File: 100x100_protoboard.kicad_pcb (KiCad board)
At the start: 2 copper layers, 97.8 x 96.5 mm, 418 parts, among them CON1 BARREL_JACK, CON2 USB_FEMALE_WITH_ID, CON3 USB_FEMALE_WITH_ID, J1 INTERCONNECT_1X03, J10 INTERCONNECT_1X03, J11 INTERCONNECT_1X03, J12 INTERCONNECT_1X03, J13 INTERCONNECT_1X03, J14 INTERCONNECT_1X03, J15 INTERCONNECT_1X03, J16 INTERCONNECT_1X03, J17 INTERCONNECT_1X03, J18 INTERCONNECT_1X03, J19 INTERCONNECT_1X03, J2 INTERCONNECT_1X03, J20 INTERCONNECT_1X03, J21 INTERCONNECT_1X03, J22 INTERCONNECT_1X03, J23 INTERCONNECT_1X03, J24 INTERCONNECT_1X03, J25 INTERCONNECT_1X03, J26 INTERCONNECT_1X03, J27 INTERCONNECT_1X03, J28 INTERCONNECT_1X03, J29 INTERCONNECT_1X03, J3 INTERCONNECT_1X03, J30 INTERCONNECT_1X03, J31 INTERCONNECT_1X03, J32 INTERCONNECT_1X03, J33 INTERCONNECT_1X03, J34 INTERCONNECT_1X03, J35 INTERCONNECT_1X03, J36 INTERCONNECT_1X03, J37 INTERCONNECT_1X03, J38 INTERCONNECT_1X03, J39 INTERCONNECT_1X03, J4 INTERCONNECT_1X03, J40 INTERCONNECT_1X03, J41 INTERCONNECT_1X03, J42 INTERCONNECT_1X03, J43 INTERCONNECT_1X03, J44 INTERCONNECT_1X03, J45 INTERCONNECT_1X03, J46 INTERCONNECT_1X03, J47 INTERCONNECT_1X03, J48 INTERCONNECT_1X03, J49 INTERCONNECT_1X03, J5 INTERCONNECT_1X03, J50 INTERCONNECT_1X03, J51 INTERCONNECT_1X03, J52 INTERCONNECT_1X03, J53 INTERCONNECT_1X03, J54 INTERCONNECT_1X03, J55 INTERCONNECT_1X03, J56 INTERCONNECT_1X03, J57 INTERCONNECT_1X03, J58 INTERCONNECT_1X03, J59 INTERCONNECT_1X03, J6 INTERCONNECT_1X03, J60 INTERCONNECT_1X03, J61 INTERCONNECT_1X03, J62 INTERCONNECT_1X03, J63 INTERCONNECT_1X03, J64 INTERCONNECT_1X03, J65 INTERCONNECT_1X02, J7 INTERCONNECT_1X03, J8 INTERCONNECT_1X03, J9 INTERCONNECT_1X03, P1 CONN_5, P1 CONN_8X2, P2 CONN_8X2, U1 LM7805CT

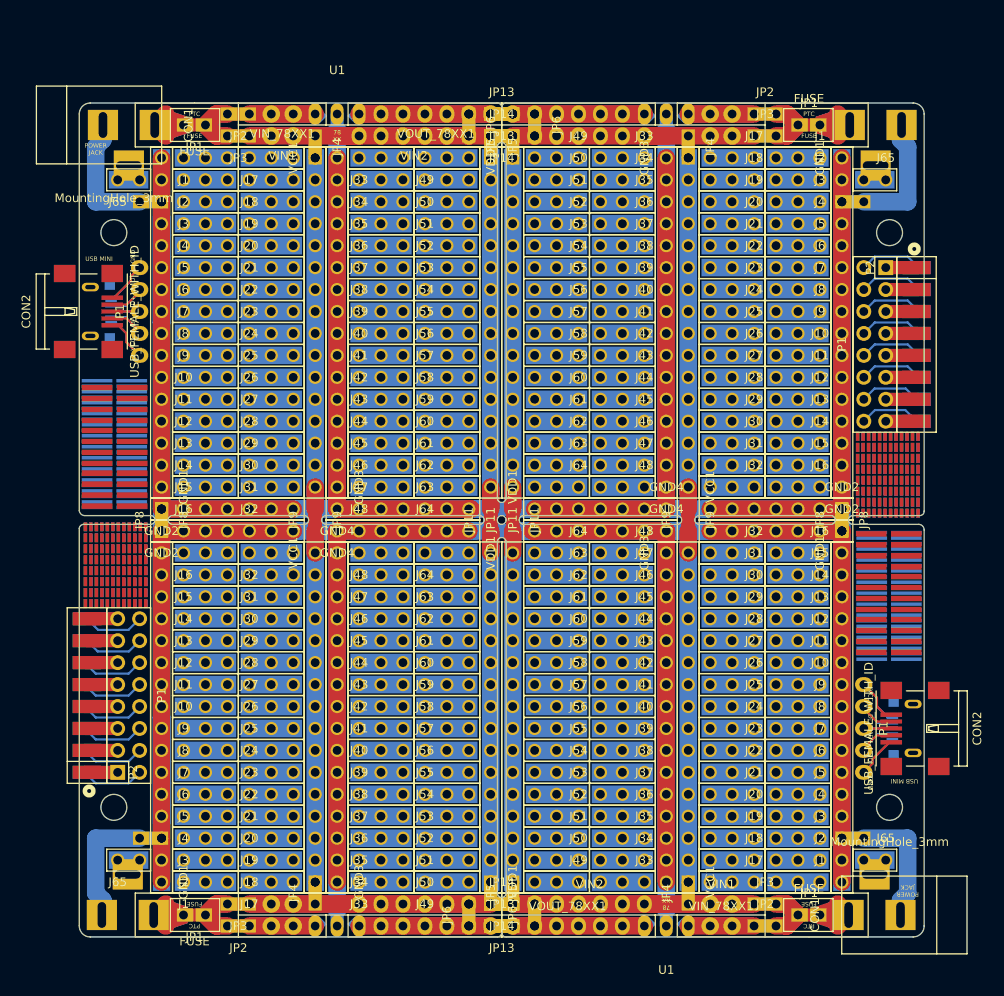
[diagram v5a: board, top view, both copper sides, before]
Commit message: rounded some corners
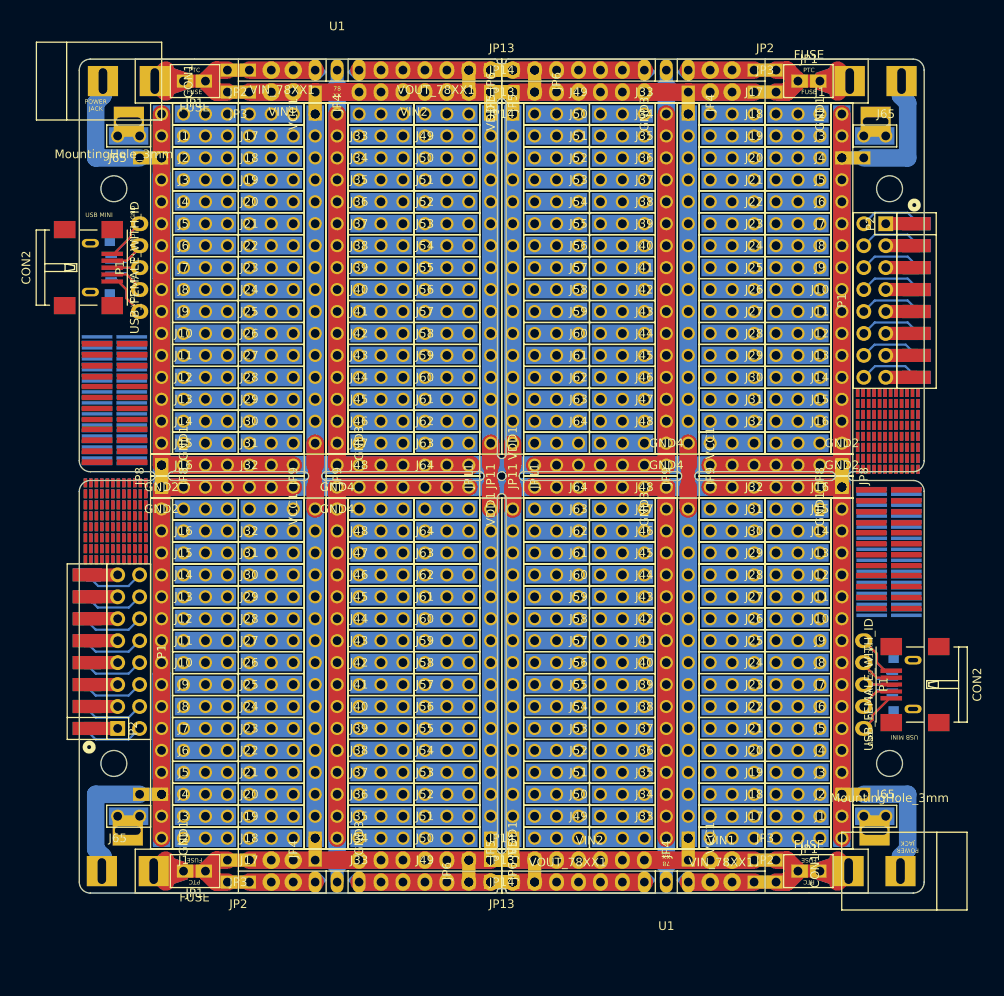
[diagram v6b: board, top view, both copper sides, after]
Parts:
- removed the C1 at (101.6, 32.8)
- removed the C1 at (101.6, 124.7)
- removed the C2 at (99.1, 32.8)
- removed the C2 at (99.1, 124.7)
- removed the CON1 at (127.8, 33.0)
- removed the CON1 at (127.6, 124.5)
- removed the CON1 at (34.8, 124.5)
- removed the F1 at (116.8, 33.0)
- removed the F1 at (116.8, 124.5)
- removed the F2 at (116.8, 33.0)
- removed the F2 at (116.8, 124.5)
- removed the GND1 at (120.7, 36.8)
- removed the GND1 at (120.7, 82.5)
- removed the GND2 at (120.7, 77.5)
- removed the GND2 at (120.7, 80.0)
- removed the GND3 at (100.3, 36.8)
- removed the GND3 at (100.3, 82.5)
- removed the GND4 at (100.3, 77.5)
- removed the GND4 at (100.3, 80.0)
- removed the J1 at (118.1, 36.8)
- removed the J1 at (118.1, 120.7)
- removed the J10 at (118.1, 59.7)
- removed the J10 at (118.1, 97.8)
- removed the J11 at (118.1, 62.2)
- removed the J11 at (118.1, 95.2)
- removed the J12 at (118.1, 64.8)
- removed the J12 at (118.1, 92.7)
- removed the J13 at (118.1, 67.3)
- removed the J13 at (118.1, 90.2)
- removed the J14 at (118.1, 69.8)
- removed the J14 at (118.1, 87.6)
- removed the J15 at (118.1, 72.4)
- removed the J15 at (118.1, 85.1)
- removed the J16 at (118.1, 74.9)
- removed the J16 at (118.1, 82.5)
- removed the J17 at (110.5, 36.8)
- removed the J17 at (110.5, 120.7)
- removed the J18 at (110.5, 39.4)
- removed the J18 at (110.5, 118.1)
- removed the J19 at (110.5, 41.9)
- removed the J19 at (110.5, 115.6)
- removed the J2 at (118.1, 39.4)
- removed the J2 at (118.1, 118.1)
- removed the J20 at (110.5, 44.5)
- removed the J20 at (110.5, 113.0)
- removed the J21 at (110.5, 47.0)
- removed the J21 at (110.5, 110.5)
- removed the J22 at (110.5, 49.5)
- removed the J22 at (110.5, 108.0)
- removed the J23 at (110.5, 52.1)
- removed the J23 at (110.5, 105.4)
- removed the J24 at (110.5, 54.6)
- removed the J24 at (110.5, 102.9)
- removed the J25 at (110.5, 57.1)
- removed the J25 at (110.5, 100.3)
- removed the J26 at (110.5, 59.7)
- removed the J26 at (110.5, 97.8)
- removed the J27 at (110.5, 62.2)
- removed the J27 at (110.5, 95.2)
- removed the J28 at (110.5, 64.8)
- removed the J28 at (110.5, 92.7)
- removed the J29 at (110.5, 67.3)
- removed the J29 at (110.5, 90.2)
- removed the J3 at (118.1, 41.9)
- removed the J3 at (118.1, 115.6)
- removed the J30 at (110.5, 69.8)
- removed the J30 at (110.5, 87.6)
- removed the J31 at (110.5, 72.4)
- removed the J31 at (110.5, 85.1)
- removed the J32 at (110.5, 74.9)
- removed the J32 at (110.5, 82.5)
- removed the J33 at (97.8, 36.8)
- removed the J33 at (97.8, 120.7)
- removed the J34 at (97.8, 39.4)
- removed the J34 at (97.8, 118.1)
- removed the J35 at (97.8, 41.9)
- removed the J35 at (97.8, 115.6)
- removed the J36 at (97.8, 44.5)
- removed the J36 at (97.8, 113.0)
- removed the J37 at (97.8, 47.0)
- removed the J37 at (97.8, 110.5)
- removed the J38 at (97.8, 49.5)
- removed the J38 at (97.8, 108.0)
- removed the J39 at (97.8, 52.1)
- removed the J39 at (97.8, 105.4)
- removed the J4 at (118.1, 44.5)
- removed the J4 at (118.1, 113.0)
- removed the J40 at (97.8, 54.6)
- removed the J40 at (97.8, 102.9)
- removed the J41 at (97.8, 57.1)
- removed the J41 at (97.8, 100.3)
- removed the J42 at (97.8, 59.7)
- removed the J42 at (97.8, 97.8)
- removed the J43 at (97.8, 62.2)
- removed the J43 at (97.8, 95.2)
- removed the J44 at (97.8, 64.8)
- removed the J44 at (97.8, 92.7)
- removed the J45 at (97.8, 67.3)
- removed the J45 at (97.8, 90.2)
- removed the J46 at (97.8, 69.8)
- removed the J46 at (97.8, 87.6)
- removed the J47 at (97.8, 72.4)
- removed the J47 at (97.8, 85.1)
- removed the J48 at (97.8, 74.9)
- removed the J48 at (97.8, 82.5)
- removed the J49 at (90.2, 36.8)
- removed the J49 at (90.2, 120.7)
- removed the J5 at (118.1, 47.0)
- removed the J5 at (118.1, 110.5)
- removed the J50 at (90.2, 39.4)
- removed the J50 at (90.2, 118.1)
- removed the J51 at (90.2, 41.9)
- removed the J51 at (90.2, 115.6)
- removed the J52 at (90.2, 44.5)
- removed the J52 at (90.2, 113.0)
- removed the J53 at (90.2, 47.0)
- removed the J53 at (90.2, 110.5)
- removed the J54 at (90.2, 49.5)
- removed the J54 at (90.2, 108.0)
- removed the J55 at (90.2, 52.1)
- removed the J55 at (90.2, 105.4)
- removed the J56 at (90.2, 54.6)
- removed the J56 at (90.2, 102.9)
- removed the J57 at (90.2, 57.1)
- removed the J57 at (90.2, 100.3)
- removed the J58 at (90.2, 59.7)
- removed the J58 at (90.2, 97.8)
- removed the J59 at (90.2, 62.2)
- removed the J59 at (90.2, 95.2)
- removed the J6 at (118.1, 49.5)
- removed the J6 at (118.1, 108.0)
- removed the J60 at (90.2, 64.8)
- removed the J60 at (90.2, 92.7)
- removed the J61 at (90.2, 67.3)
- removed the J61 at (90.2, 90.2)
- removed the J62 at (90.2, 69.8)
- removed the J62 at (90.2, 87.6)
- removed the J63 at (90.2, 72.4)
- removed the J63 at (90.2, 85.1)
- removed the J64 at (90.2, 74.9)
- removed the J64 at (90.2, 82.5)
- removed the J65 at (125.7, 39.4)
- removed the J65 at (125.7, 118.1)
- removed the J7 at (118.1, 52.1)
- removed the J7 at (118.1, 105.4)
- removed the J8 at (118.1, 54.6)
- removed the J8 at (118.1, 102.9)
- removed the J9 at (118.1, 57.1)
- removed the J9 at (118.1, 100.3)
- removed the JP1 at (116.8, 33.0)
- removed the JP1 at (116.8, 124.5)
- removed the JP10 at (82.5, 78.7) (x2)
- removed the JP11 at (82.5, 78.7) (x2)
- removed the JP12 at (81.3, 77.5)
- removed the JP12 at (81.3, 80.0)
- removed the JP13 at (81.3, 31.8)
- removed the JP13 at (81.3, 125.7)
- removed the JP14 at (81.3, 34.3)
- removed the JP14 at (81.3, 123.2)
- removed the JP15 at (102.9, 78.7) (x2)
- removed the JP2 at (111.8, 31.8)
- removed the JP2 at (111.8, 125.7)
- removed the JP3 at (111.8, 34.3)
- removed the JP3 at (111.8, 123.2)
- removed the JP4 at (102.9, 35.6)
- removed the JP4 at (102.9, 121.9)
- removed the JP5 at (82.5, 35.6)
- removed the JP5 at (82.5, 121.9)
- removed the JP6 at (85.1, 33.0)
- removed the JP6 at (85.1, 124.5)
- removed the JP7 at (121.9, 41.9)
- removed the JP7 at (121.9, 115.6)
- removed the JP8 at (120.7, 78.7) (x2)
- removed the JP9 at (102.9, 78.7) (x2)
- removed the MountingHole_3mm at (126.2, 45.5)
- removed the MountingHole_3mm at (126.2, 112.0)
- removed the P1 at (124.5, 58.4)
- removed the P1 at (123.2, 102.9)
- removed the Ref** at (126.6, 76.0) (x2)
- removed the Ref** at (126.1, 92.6)
- removed the Ref** at (126.6, 71.0) (x2)
- removed the Ref** at (126.1, 92.2)
- removed the Ref** at (126.1, 87.2)
- removed the Ref** at (126.1, 82.2)
- removed the Ref** at (126.1, 82.4)
- removed the Ref** at (126.1, 87.5)
- removed the U1 at (100.3, 31.8)
- removed the U1 at (100.3, 125.7)
- removed the VCC1 at (102.9, 74.9)
- removed the VCC1 at (102.9, 120.7)
- removed the VDD1 at (82.5, 36.8)
- removed the VDD1 at (82.5, 82.5)
- removed the VIN1 at (106.7, 34.3)
- removed the VIN1 at (106.7, 123.2)
- removed the VIN2 at (91.4, 34.3)
- removed the VIN2 at (91.4, 123.2)
- removed the VIN_78XX1 at (106.7, 31.8)
- removed the VIN_78XX1 at (106.7, 125.7)
- removed the VOUT_78XX1 at (88.9, 31.8)
- removed the VOUT_78XX1 at (88.9, 125.7)
- added C1: u33, Capacitors_SMD:C_0805_HandSoldering, B.Cu at (101.6, 27.7)
- added C1: u33, Capacitors_SMD:C_0805_HandSoldering, B.Cu at (101.6, 119.6)
- added C2: u1, Capacitors_SMD:C_0805_HandSoldering, B.Cu at (99.1, 27.7)
- added C2: u1, Capacitors_SMD:C_0805_HandSoldering, B.Cu at (99.1, 119.6)
- added CON1: BARREL_JACK, Connect:BARREL_JACK, B.Cu at (127.8, 27.9)
- added CON1: BARREL_JACK, Connect:BARREL_JACK, F.Cu at (127.6, 119.4)
- added CON1: BARREL_JACK, Connect:BARREL_JACK, B.Cu at (34.8, 119.4)
- added F1: FUSE, Muonde:CC12ZZ, B.Cu at (116.8, 27.9)
- added F1: FUSE, Muonde:CC12ZZ, F.Cu at (116.8, 119.4)
- added F2: FUSE, Muonde:CC12ZZ, F.Cu at (116.8, 27.9)
- added F2: FUSE, Muonde:CC12ZZ, B.Cu at (116.8, 119.4)
- added GND1: INTERCONNECT_1X16, 2.54mm_Pin_Headers:Interconnect_1x16, F.Cu at (120.7, 31.8)
- added GND1: INTERCONNECT_1X16, 2.54mm_Pin_Headers:Interconnect_1x16, F.Cu at (120.7, 77.5)
- added GND2: INTERCONNECT_1X07, 2.54mm_Pin_Headers:Interconnect_1x07, F.Cu at (120.7, 72.4)
- added GND2: INTERCONNECT_1X07, 2.54mm_Pin_Headers:Interconnect_1x07, F.Cu at (120.7, 74.9)
- added GND3: INTERCONNECT_1X16, 2.54mm_Pin_Headers:Interconnect_1x16, F.Cu at (100.3, 31.8)
- added GND3: INTERCONNECT_1X16, 2.54mm_Pin_Headers:Interconnect_1x16, F.Cu at (100.3, 77.5)
- added GND4: INTERCONNECT_1X07, 2.54mm_Pin_Headers:Interconnect_1x07, F.Cu at (100.3, 72.4)
- added GND4: INTERCONNECT_1X07, 2.54mm_Pin_Headers:Interconnect_1x07, F.Cu at (100.3, 74.9)
- added J1: INTERCONNECT_1X03, 2.54mm_Pin_Headers:Interconnect_1x03, F.Cu at (118.1, 31.8)
- added J1: INTERCONNECT_1X03, 2.54mm_Pin_Headers:Interconnect_1x03, F.Cu at (118.1, 115.6)
- added J10: INTERCONNECT_1X03, 2.54mm_Pin_Headers:Interconnect_1x03, F.Cu at (118.1, 54.6)
- added J10: INTERCONNECT_1X03, 2.54mm_Pin_Headers:Interconnect_1x03, F.Cu at (118.1, 92.7)
- added J11: INTERCONNECT_1X03, 2.54mm_Pin_Headers:Interconnect_1x03, F.Cu at (118.1, 57.1)
- added J11: INTERCONNECT_1X03, 2.54mm_Pin_Headers:Interconnect_1x03, F.Cu at (118.1, 90.2)
- added J12: INTERCONNECT_1X03, 2.54mm_Pin_Headers:Interconnect_1x03, F.Cu at (118.1, 59.7)
- added J12: INTERCONNECT_1X03, 2.54mm_Pin_Headers:Interconnect_1x03, F.Cu at (118.1, 87.6)
- added J13: INTERCONNECT_1X03, 2.54mm_Pin_Headers:Interconnect_1x03, F.Cu at (118.1, 62.2)
- added J13: INTERCONNECT_1X03, 2.54mm_Pin_Headers:Interconnect_1x03, F.Cu at (118.1, 85.1)
- added J14: INTERCONNECT_1X03, 2.54mm_Pin_Headers:Interconnect_1x03, F.Cu at (118.1, 64.8)
- added J14: INTERCONNECT_1X03, 2.54mm_Pin_Headers:Interconnect_1x03, F.Cu at (118.1, 82.5)
- added J15: INTERCONNECT_1X03, 2.54mm_Pin_Headers:Interconnect_1x03, F.Cu at (118.1, 67.3)
- added J15: INTERCONNECT_1X03, 2.54mm_Pin_Headers:Interconnect_1x03, F.Cu at (118.1, 80.0)
- added J16: INTERCONNECT_1X03, 2.54mm_Pin_Headers:Interconnect_1x03, F.Cu at (118.1, 69.8)
- added J16: INTERCONNECT_1X03, 2.54mm_Pin_Headers:Interconnect_1x03, F.Cu at (118.1, 77.5)
- added J17: INTERCONNECT_1X03, 2.54mm_Pin_Headers:Interconnect_1x03, F.Cu at (110.5, 31.8)
- added J17: INTERCONNECT_1X03, 2.54mm_Pin_Headers:Interconnect_1x03, F.Cu at (110.5, 115.6)
- added J18: INTERCONNECT_1X03, 2.54mm_Pin_Headers:Interconnect_1x03, F.Cu at (110.5, 34.3)
- added J18: INTERCONNECT_1X03, 2.54mm_Pin_Headers:Interconnect_1x03, F.Cu at (110.5, 113.0)
- added J19: INTERCONNECT_1X03, 2.54mm_Pin_Headers:Interconnect_1x03, F.Cu at (110.5, 36.8)
- added J19: INTERCONNECT_1X03, 2.54mm_Pin_Headers:Interconnect_1x03, F.Cu at (110.5, 110.5)
- added J2: INTERCONNECT_1X03, 2.54mm_Pin_Headers:Interconnect_1x03, F.Cu at (118.1, 34.3)
- added J2: INTERCONNECT_1X03, 2.54mm_Pin_Headers:Interconnect_1x03, F.Cu at (118.1, 113.0)
- added J20: INTERCONNECT_1X03, 2.54mm_Pin_Headers:Interconnect_1x03, F.Cu at (110.5, 39.4)
- added J20: INTERCONNECT_1X03, 2.54mm_Pin_Headers:Interconnect_1x03, F.Cu at (110.5, 108.0)
- added J21: INTERCONNECT_1X03, 2.54mm_Pin_Headers:Interconnect_1x03, F.Cu at (110.5, 41.9)
- added J21: INTERCONNECT_1X03, 2.54mm_Pin_Headers:Interconnect_1x03, F.Cu at (110.5, 105.4)
- added J22: INTERCONNECT_1X03, 2.54mm_Pin_Headers:Interconnect_1x03, F.Cu at (110.5, 44.5)
- added J22: INTERCONNECT_1X03, 2.54mm_Pin_Headers:Interconnect_1x03, F.Cu at (110.5, 102.9)
- added J23: INTERCONNECT_1X03, 2.54mm_Pin_Headers:Interconnect_1x03, F.Cu at (110.5, 47.0)
- added J23: INTERCONNECT_1X03, 2.54mm_Pin_Headers:Interconnect_1x03, F.Cu at (110.5, 100.3)
- added J24: INTERCONNECT_1X03, 2.54mm_Pin_Headers:Interconnect_1x03, F.Cu at (110.5, 49.5)
- added J24: INTERCONNECT_1X03, 2.54mm_Pin_Headers:Interconnect_1x03, F.Cu at (110.5, 97.8)
- added J25: INTERCONNECT_1X03, 2.54mm_Pin_Headers:Interconnect_1x03, F.Cu at (110.5, 52.1)
- added J25: INTERCONNECT_1X03, 2.54mm_Pin_Headers:Interconnect_1x03, F.Cu at (110.5, 95.2)
- added J26: INTERCONNECT_1X03, 2.54mm_Pin_Headers:Interconnect_1x03, F.Cu at (110.5, 54.6)
- added J26: INTERCONNECT_1X03, 2.54mm_Pin_Headers:Interconnect_1x03, F.Cu at (110.5, 92.7)
- added J27: INTERCONNECT_1X03, 2.54mm_Pin_Headers:Interconnect_1x03, F.Cu at (110.5, 57.1)
- added J27: INTERCONNECT_1X03, 2.54mm_Pin_Headers:Interconnect_1x03, F.Cu at (110.5, 90.2)
- added J28: INTERCONNECT_1X03, 2.54mm_Pin_Headers:Interconnect_1x03, F.Cu at (110.5, 59.7)
- added J28: INTERCONNECT_1X03, 2.54mm_Pin_Headers:Interconnect_1x03, F.Cu at (110.5, 87.6)
- added J29: INTERCONNECT_1X03, 2.54mm_Pin_Headers:Interconnect_1x03, F.Cu at (110.5, 62.2)
- added J29: INTERCONNECT_1X03, 2.54mm_Pin_Headers:Interconnect_1x03, F.Cu at (110.5, 85.1)
- added J3: INTERCONNECT_1X03, 2.54mm_Pin_Headers:Interconnect_1x03, F.Cu at (118.1, 36.8)
- added J3: INTERCONNECT_1X03, 2.54mm_Pin_Headers:Interconnect_1x03, F.Cu at (118.1, 110.5)
- added J30: INTERCONNECT_1X03, 2.54mm_Pin_Headers:Interconnect_1x03, F.Cu at (110.5, 64.8)
- added J30: INTERCONNECT_1X03, 2.54mm_Pin_Headers:Interconnect_1x03, F.Cu at (110.5, 82.5)
- added J31: INTERCONNECT_1X03, 2.54mm_Pin_Headers:Interconnect_1x03, F.Cu at (110.5, 67.3)
- added J31: INTERCONNECT_1X03, 2.54mm_Pin_Headers:Interconnect_1x03, F.Cu at (110.5, 80.0)
- added J32: INTERCONNECT_1X03, 2.54mm_Pin_Headers:Interconnect_1x03, F.Cu at (110.5, 69.8)
- added J32: INTERCONNECT_1X03, 2.54mm_Pin_Headers:Interconnect_1x03, F.Cu at (110.5, 77.5)
- added J33: INTERCONNECT_1X03, 2.54mm_Pin_Headers:Interconnect_1x03, F.Cu at (97.8, 31.8)
- added J33: INTERCONNECT_1X03, 2.54mm_Pin_Headers:Interconnect_1x03, F.Cu at (97.8, 115.6)
- added J34: INTERCONNECT_1X03, 2.54mm_Pin_Headers:Interconnect_1x03, F.Cu at (97.8, 34.3)
- added J34: INTERCONNECT_1X03, 2.54mm_Pin_Headers:Interconnect_1x03, F.Cu at (97.8, 113.0)
- added J35: INTERCONNECT_1X03, 2.54mm_Pin_Headers:Interconnect_1x03, F.Cu at (97.8, 36.8)
- added J35: INTERCONNECT_1X03, 2.54mm_Pin_Headers:Interconnect_1x03, F.Cu at (97.8, 110.5)
- added J36: INTERCONNECT_1X03, 2.54mm_Pin_Headers:Interconnect_1x03, F.Cu at (97.8, 39.4)
- added J36: INTERCONNECT_1X03, 2.54mm_Pin_Headers:Interconnect_1x03, F.Cu at (97.8, 108.0)
- added J37: INTERCONNECT_1X03, 2.54mm_Pin_Headers:Interconnect_1x03, F.Cu at (97.8, 41.9)
- added J37: INTERCONNECT_1X03, 2.54mm_Pin_Headers:Interconnect_1x03, F.Cu at (97.8, 105.4)
- added J38: INTERCONNECT_1X03, 2.54mm_Pin_Headers:Interconnect_1x03, F.Cu at (97.8, 44.5)
- added J38: INTERCONNECT_1X03, 2.54mm_Pin_Headers:Interconnect_1x03, F.Cu at (97.8, 102.9)
- added J39: INTERCONNECT_1X03, 2.54mm_Pin_Headers:Interconnect_1x03, F.Cu at (97.8, 47.0)
- added J39: INTERCONNECT_1X03, 2.54mm_Pin_Headers:Interconnect_1x03, F.Cu at (97.8, 100.3)
- added J4: INTERCONNECT_1X03, 2.54mm_Pin_Headers:Interconnect_1x03, F.Cu at (118.1, 39.4)
- added J4: INTERCONNECT_1X03, 2.54mm_Pin_Headers:Interconnect_1x03, F.Cu at (118.1, 108.0)
- added J40: INTERCONNECT_1X03, 2.54mm_Pin_Headers:Interconnect_1x03, F.Cu at (97.8, 49.5)
- added J40: INTERCONNECT_1X03, 2.54mm_Pin_Headers:Interconnect_1x03, F.Cu at (97.8, 97.8)
- added J41: INTERCONNECT_1X03, 2.54mm_Pin_Headers:Interconnect_1x03, F.Cu at (97.8, 52.1)
- added J41: INTERCONNECT_1X03, 2.54mm_Pin_Headers:Interconnect_1x03, F.Cu at (97.8, 95.2)
- added J42: INTERCONNECT_1X03, 2.54mm_Pin_Headers:Interconnect_1x03, F.Cu at (97.8, 54.6)
- added J42: INTERCONNECT_1X03, 2.54mm_Pin_Headers:Interconnect_1x03, F.Cu at (97.8, 92.7)
- added J43: INTERCONNECT_1X03, 2.54mm_Pin_Headers:Interconnect_1x03, F.Cu at (97.8, 57.1)
- added J43: INTERCONNECT_1X03, 2.54mm_Pin_Headers:Interconnect_1x03, F.Cu at (97.8, 90.2)
- added J44: INTERCONNECT_1X03, 2.54mm_Pin_Headers:Interconnect_1x03, F.Cu at (97.8, 59.7)
- added J44: INTERCONNECT_1X03, 2.54mm_Pin_Headers:Interconnect_1x03, F.Cu at (97.8, 87.6)
- added J45: INTERCONNECT_1X03, 2.54mm_Pin_Headers:Interconnect_1x03, F.Cu at (97.8, 62.2)
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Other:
- outline, holes or cut-outs redrawn

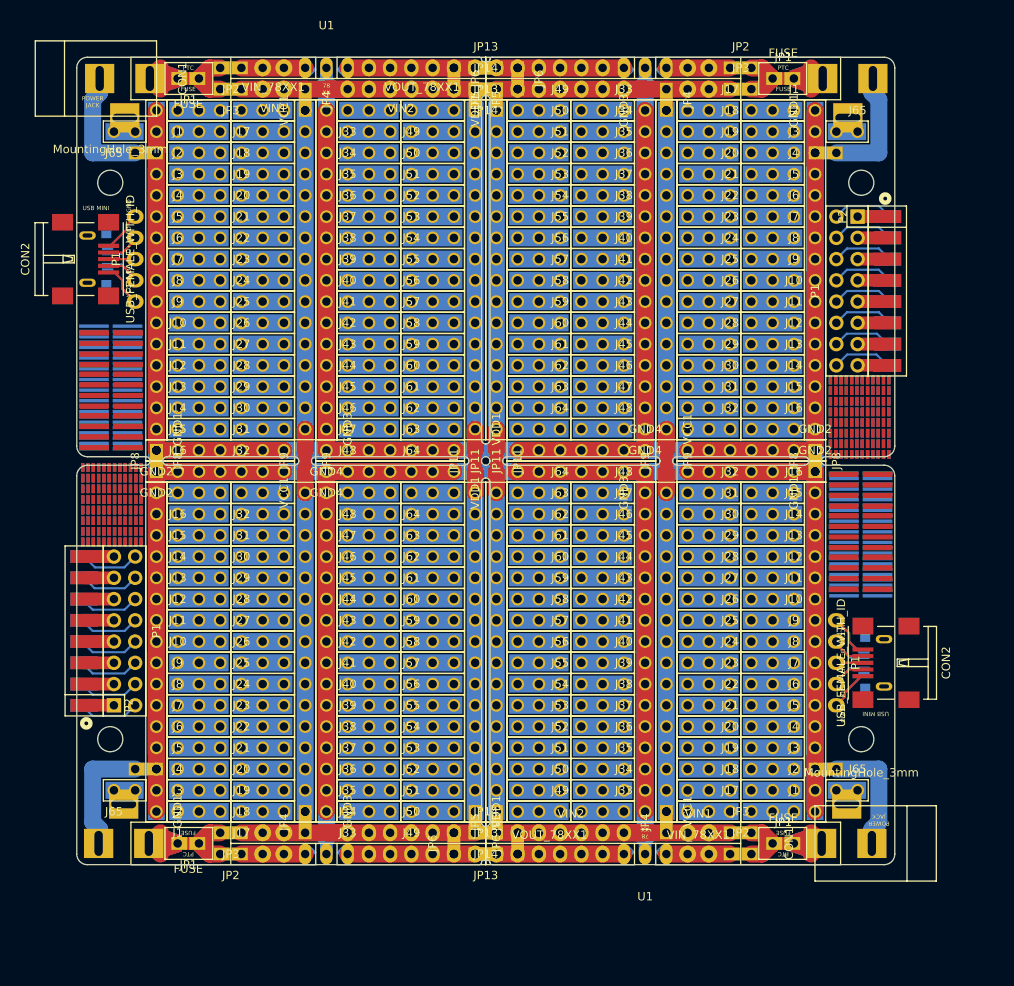
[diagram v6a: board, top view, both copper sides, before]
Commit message: increased the size of 78XX capacitor values, so that they are readable and flipped 78XX text on bottom left so that it does not conflict with capacitor pads
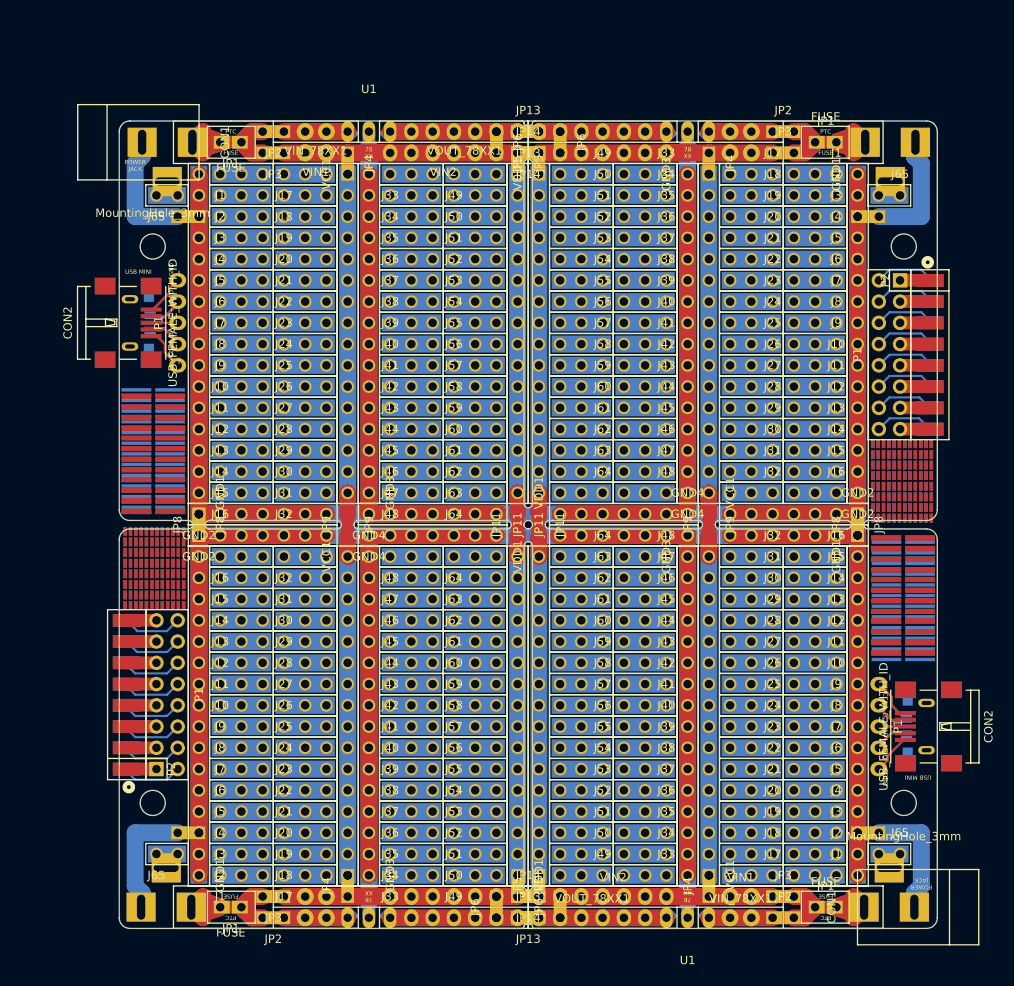
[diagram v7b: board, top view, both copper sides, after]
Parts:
- removed the C1 at (101.6, 27.7)
- removed the C1 at (101.6, 119.6)
- removed the C2 at (99.1, 27.7)
- removed the C2 at (99.1, 119.6)
- removed the CON1 at (127.8, 27.9)
- removed the CON1 at (127.6, 119.4)
- removed the F1 at (116.8, 27.9)
- removed the F1 at (116.8, 119.4)
- removed the F2 at (116.8, 27.9)
- removed the F2 at (116.8, 119.4)
- removed the GND1 at (120.7, 31.8)
- removed the GND1 at (120.7, 77.5)
- removed the GND2 at (120.7, 72.4)
- removed the GND2 at (120.7, 74.9)
- removed the GND3 at (100.3, 31.8)
- removed the GND3 at (100.3, 77.5)
- removed the GND4 at (100.3, 72.4)
- removed the GND4 at (100.3, 74.9)
- removed the J1 at (118.1, 31.8)
- removed the J1 at (118.1, 115.6)
- removed the J10 at (118.1, 54.6)
- removed the J10 at (118.1, 92.7)
- removed the J11 at (118.1, 57.1)
- removed the J11 at (118.1, 90.2)
- removed the J12 at (118.1, 59.7)
- removed the J12 at (118.1, 87.6)
- removed the J13 at (118.1, 62.2)
- removed the J13 at (118.1, 85.1)
- removed the J14 at (118.1, 64.8)
- removed the J14 at (118.1, 82.5)
- removed the J15 at (118.1, 67.3)
- removed the J15 at (118.1, 80.0)
- removed the J16 at (118.1, 69.8)
- removed the J16 at (118.1, 77.5)
- removed the J17 at (110.5, 31.8)
- removed the J17 at (110.5, 115.6)
- removed the J18 at (110.5, 34.3)
- removed the J18 at (110.5, 113.0)
- removed the J19 at (110.5, 36.8)
- removed the J19 at (110.5, 110.5)
- removed the J2 at (118.1, 34.3)
- removed the J2 at (118.1, 113.0)
- removed the J20 at (110.5, 39.4)
- removed the J20 at (110.5, 108.0)
- removed the J21 at (110.5, 41.9)
- removed the J21 at (110.5, 105.4)
- removed the J22 at (110.5, 44.5)
- removed the J22 at (110.5, 102.9)
- removed the J23 at (110.5, 47.0)
- removed the J23 at (110.5, 100.3)
- removed the J24 at (110.5, 49.5)
- removed the J24 at (110.5, 97.8)
- removed the J25 at (110.5, 52.1)
- removed the J25 at (110.5, 95.2)
- removed the J26 at (110.5, 54.6)
- removed the J26 at (110.5, 92.7)
- removed the J27 at (110.5, 57.1)
- removed the J27 at (110.5, 90.2)
- removed the J28 at (110.5, 59.7)
- removed the J28 at (110.5, 87.6)
- removed the J29 at (110.5, 62.2)
- removed the J29 at (110.5, 85.1)
- removed the J3 at (118.1, 36.8)
- removed the J3 at (118.1, 110.5)
- removed the J30 at (110.5, 64.8)
- removed the J30 at (110.5, 82.5)
- removed the J31 at (110.5, 67.3)
- removed the J31 at (110.5, 80.0)
- removed the J32 at (110.5, 69.8)
- removed the J32 at (110.5, 77.5)
- removed the J33 at (97.8, 31.8)
- removed the J33 at (97.8, 115.6)
- removed the J34 at (97.8, 34.3)
- removed the J34 at (97.8, 113.0)
- removed the J35 at (97.8, 36.8)
- removed the J35 at (97.8, 110.5)
- removed the J36 at (97.8, 39.4)
- removed the J36 at (97.8, 108.0)
- removed the J37 at (97.8, 41.9)
- removed the J37 at (97.8, 105.4)
- removed the J38 at (97.8, 44.5)
- removed the J38 at (97.8, 102.9)
- removed the J39 at (97.8, 47.0)
- removed the J39 at (97.8, 100.3)
- removed the J4 at (118.1, 39.4)
- removed the J4 at (118.1, 108.0)
- removed the J40 at (97.8, 49.5)
- removed the J40 at (97.8, 97.8)
- removed the J41 at (97.8, 52.1)
- removed the J41 at (97.8, 95.2)
- removed the J42 at (97.8, 54.6)
- removed the J42 at (97.8, 92.7)
- removed the J43 at (97.8, 57.1)
- removed the J43 at (97.8, 90.2)
- removed the J44 at (97.8, 59.7)
- removed the J44 at (97.8, 87.6)
- removed the J45 at (97.8, 62.2)
- removed the J45 at (97.8, 85.1)
- removed the J46 at (97.8, 64.8)
- removed the J46 at (97.8, 82.5)
- removed the J47 at (97.8, 67.3)
- removed the J47 at (97.8, 80.0)
- removed the J48 at (97.8, 69.8)
- removed the J48 at (97.8, 77.5)
- removed the J49 at (90.2, 31.8)
- removed the J49 at (90.2, 115.6)
- removed the J5 at (118.1, 41.9)
- removed the J5 at (118.1, 105.4)
- removed the J50 at (90.2, 34.3)
- removed the J50 at (90.2, 113.0)
- removed the J51 at (90.2, 36.8)
- removed the J51 at (90.2, 110.5)
- removed the J52 at (90.2, 39.4)
- removed the J52 at (90.2, 108.0)
- removed the J53 at (90.2, 41.9)
- removed the J53 at (90.2, 105.4)
- removed the J54 at (90.2, 44.5)
- removed the J54 at (90.2, 102.9)
- removed the J55 at (90.2, 47.0)
- removed the J55 at (90.2, 100.3)
- removed the J56 at (90.2, 49.5)
- removed the J56 at (90.2, 97.8)
- removed the J57 at (90.2, 52.1)
- removed the J57 at (90.2, 95.2)
- removed the J58 at (90.2, 54.6)
- removed the J58 at (90.2, 92.7)
- removed the J59 at (90.2, 57.1)
- removed the J59 at (90.2, 90.2)
- removed the J6 at (118.1, 44.5)
- removed the J6 at (118.1, 102.9)
- removed the J60 at (90.2, 59.7)
- removed the J60 at (90.2, 87.6)
- removed the J61 at (90.2, 62.2)
- removed the J61 at (90.2, 85.1)
- removed the J62 at (90.2, 64.8)
- removed the J62 at (90.2, 82.5)
- removed the J63 at (90.2, 67.3)
- removed the J63 at (90.2, 80.0)
- removed the J64 at (90.2, 69.8)
- removed the J64 at (90.2, 77.5)
- removed the J65 at (125.7, 34.3)
- removed the J65 at (125.7, 113.0)
- removed the J7 at (118.1, 47.0)
- removed the J7 at (118.1, 100.3)
- removed the J8 at (118.1, 49.5)
- removed the J8 at (118.1, 97.8)
- removed the J9 at (118.1, 52.1)
- removed the J9 at (118.1, 95.2)
- removed the JP1 at (116.8, 27.9)
- removed the JP1 at (116.8, 119.4)
- removed the JP10 at (82.5, 73.7) (x2)
- removed the JP11 at (82.5, 73.7) (x2)
- removed the JP12 at (81.3, 72.4)
- removed the JP12 at (81.3, 74.9)
- removed the JP13 at (81.3, 26.7)
- removed the JP13 at (81.3, 120.7)
- removed the JP14 at (81.3, 29.2)
- removed the JP14 at (81.3, 118.1)
- removed the JP15 at (102.9, 73.7) (x2)
- removed the JP2 at (111.8, 26.7)
- removed the JP2 at (111.8, 120.7)
- removed the JP3 at (111.8, 29.2)
- removed the JP3 at (111.8, 118.1)
- removed the JP4 at (102.9, 30.5)
- removed the JP4 at (102.9, 116.8)
- removed the JP5 at (82.5, 30.5)
- removed the JP5 at (82.5, 116.8)
- removed the JP6 at (85.1, 27.9)
- removed the JP6 at (85.1, 119.4)
- removed the JP7 at (121.9, 36.8)
- removed the JP7 at (121.9, 110.5)
- removed the JP8 at (120.7, 73.7) (x2)
- removed the JP9 at (102.9, 73.7) (x2)
- removed the MountingHole_3mm at (126.2, 40.4)
- removed the MountingHole_3mm at (126.2, 106.9)
- removed the P1 at (124.5, 53.3)
- removed the P1 at (123.2, 97.8)
- removed the Ref** at (126.6, 71.0) (x2)
- removed the Ref** at (126.1, 87.6)
- removed the Ref** at (126.6, 65.9) (x2)
- removed the Ref** at (126.1, 87.1)
- removed the Ref** at (126.1, 82.1)
- removed the Ref** at (126.1, 77.2)
- removed the Ref** at (126.1, 77.3)
- removed the Ref** at (126.1, 82.4)
- removed the U1 at (100.3, 26.7)
- removed the U1 at (100.3, 120.7)
- removed the VCC1 at (102.9, 69.8)
- removed the VCC1 at (102.9, 115.6)
- removed the VDD1 at (82.5, 31.8)
- removed the VDD1 at (82.5, 77.5)
- removed the VIN1 at (106.7, 29.2)
- removed the VIN1 at (106.7, 118.1)
- removed the VIN2 at (91.4, 29.2)
- removed the VIN2 at (91.4, 118.1)
- removed the VIN_78XX1 at (106.7, 26.7)
- removed the VIN_78XX1 at (106.7, 120.7)
- removed the VOUT_78XX1 at (88.9, 26.7)
- removed the VOUT_78XX1 at (88.9, 120.7)
- added C1: u33, Capacitors_SMD:C_0805_HandSoldering, B.Cu at (106.7, 35.3)
- added C1: u33, Capacitors_SMD:C_0805_HandSoldering, B.Cu at (106.7, 127.3)
- added C2: u1, Capacitors_SMD:C_0805_HandSoldering, B.Cu at (104.1, 35.3)
- added C2: u1, Capacitors_SMD:C_0805_HandSoldering, B.Cu at (104.1, 127.3)
- added CON1: BARREL_JACK, Connect:BARREL_JACK, B.Cu at (132.8, 35.6)
- added CON1: BARREL_JACK, Connect:BARREL_JACK, F.Cu at (132.7, 127.0)
- added F1: FUSE, Muonde:CC12ZZ, B.Cu at (121.9, 35.6)
- added F1: FUSE, Muonde:CC12ZZ, F.Cu at (121.9, 127.0)
- added F2: FUSE, Muonde:CC12ZZ, F.Cu at (121.9, 35.6)
- added F2: FUSE, Muonde:CC12ZZ, B.Cu at (121.9, 127.0)
- added GND1: INTERCONNECT_1X16, 2.54mm_Pin_Headers:Interconnect_1x16, F.Cu at (125.7, 39.4)
- added GND1: INTERCONNECT_1X16, 2.54mm_Pin_Headers:Interconnect_1x16, F.Cu at (125.7, 85.1)
- added GND2: INTERCONNECT_1X07, 2.54mm_Pin_Headers:Interconnect_1x07, F.Cu at (125.7, 80.0)
- added GND2: INTERCONNECT_1X07, 2.54mm_Pin_Headers:Interconnect_1x07, F.Cu at (125.7, 82.5)
- added GND3: INTERCONNECT_1X16, 2.54mm_Pin_Headers:Interconnect_1x16, F.Cu at (105.4, 39.4)
- added GND3: INTERCONNECT_1X16, 2.54mm_Pin_Headers:Interconnect_1x16, F.Cu at (105.4, 85.1)
- added GND4: INTERCONNECT_1X07, 2.54mm_Pin_Headers:Interconnect_1x07, F.Cu at (105.4, 80.0)
- added GND4: INTERCONNECT_1X07, 2.54mm_Pin_Headers:Interconnect_1x07, F.Cu at (105.4, 82.5)
- added J1: INTERCONNECT_1X03, 2.54mm_Pin_Headers:Interconnect_1x03, F.Cu at (123.2, 39.4)
- added J1: INTERCONNECT_1X03, 2.54mm_Pin_Headers:Interconnect_1x03, F.Cu at (123.2, 123.2)
- added J10: INTERCONNECT_1X03, 2.54mm_Pin_Headers:Interconnect_1x03, F.Cu at (123.2, 62.2)
- added J10: INTERCONNECT_1X03, 2.54mm_Pin_Headers:Interconnect_1x03, F.Cu at (123.2, 100.3)
- added J11: INTERCONNECT_1X03, 2.54mm_Pin_Headers:Interconnect_1x03, F.Cu at (123.2, 64.8)
- added J11: INTERCONNECT_1X03, 2.54mm_Pin_Headers:Interconnect_1x03, F.Cu at (123.2, 97.8)
- added J12: INTERCONNECT_1X03, 2.54mm_Pin_Headers:Interconnect_1x03, F.Cu at (123.2, 67.3)
- added J12: INTERCONNECT_1X03, 2.54mm_Pin_Headers:Interconnect_1x03, F.Cu at (123.2, 95.2)
- added J13: INTERCONNECT_1X03, 2.54mm_Pin_Headers:Interconnect_1x03, F.Cu at (123.2, 69.8)
- added J13: INTERCONNECT_1X03, 2.54mm_Pin_Headers:Interconnect_1x03, F.Cu at (123.2, 92.7)
- added J14: INTERCONNECT_1X03, 2.54mm_Pin_Headers:Interconnect_1x03, F.Cu at (123.2, 72.4)
- added J14: INTERCONNECT_1X03, 2.54mm_Pin_Headers:Interconnect_1x03, F.Cu at (123.2, 90.2)
- added J15: INTERCONNECT_1X03, 2.54mm_Pin_Headers:Interconnect_1x03, F.Cu at (123.2, 74.9)
- added J15: INTERCONNECT_1X03, 2.54mm_Pin_Headers:Interconnect_1x03, F.Cu at (123.2, 87.6)
- added J16: INTERCONNECT_1X03, 2.54mm_Pin_Headers:Interconnect_1x03, F.Cu at (123.2, 77.5)
- added J16: INTERCONNECT_1X03, 2.54mm_Pin_Headers:Interconnect_1x03, F.Cu at (123.2, 85.1)
- added J17: INTERCONNECT_1X03, 2.54mm_Pin_Headers:Interconnect_1x03, F.Cu at (115.6, 39.4)
- added J17: INTERCONNECT_1X03, 2.54mm_Pin_Headers:Interconnect_1x03, F.Cu at (115.6, 123.2)
- added J18: INTERCONNECT_1X03, 2.54mm_Pin_Headers:Interconnect_1x03, F.Cu at (115.6, 41.9)
- added J18: INTERCONNECT_1X03, 2.54mm_Pin_Headers:Interconnect_1x03, F.Cu at (115.6, 120.7)
- added J19: INTERCONNECT_1X03, 2.54mm_Pin_Headers:Interconnect_1x03, F.Cu at (115.6, 44.5)
- added J19: INTERCONNECT_1X03, 2.54mm_Pin_Headers:Interconnect_1x03, F.Cu at (115.6, 118.1)
- added J2: INTERCONNECT_1X03, 2.54mm_Pin_Headers:Interconnect_1x03, F.Cu at (123.2, 41.9)
- added J2: INTERCONNECT_1X03, 2.54mm_Pin_Headers:Interconnect_1x03, F.Cu at (123.2, 120.7)
- added J20: INTERCONNECT_1X03, 2.54mm_Pin_Headers:Interconnect_1x03, F.Cu at (115.6, 47.0)
- added J20: INTERCONNECT_1X03, 2.54mm_Pin_Headers:Interconnect_1x03, F.Cu at (115.6, 115.6)
- added J21: INTERCONNECT_1X03, 2.54mm_Pin_Headers:Interconnect_1x03, F.Cu at (115.6, 49.5)
- added J21: INTERCONNECT_1X03, 2.54mm_Pin_Headers:Interconnect_1x03, F.Cu at (115.6, 113.0)
- added J22: INTERCONNECT_1X03, 2.54mm_Pin_Headers:Interconnect_1x03, F.Cu at (115.6, 52.1)
- added J22: INTERCONNECT_1X03, 2.54mm_Pin_Headers:Interconnect_1x03, F.Cu at (115.6, 110.5)
- added J23: INTERCONNECT_1X03, 2.54mm_Pin_Headers:Interconnect_1x03, F.Cu at (115.6, 54.6)
- added J23: INTERCONNECT_1X03, 2.54mm_Pin_Headers:Interconnect_1x03, F.Cu at (115.6, 108.0)
- added J24: INTERCONNECT_1X03, 2.54mm_Pin_Headers:Interconnect_1x03, F.Cu at (115.6, 57.1)
- added J24: INTERCONNECT_1X03, 2.54mm_Pin_Headers:Interconnect_1x03, F.Cu at (115.6, 105.4)
- added J25: INTERCONNECT_1X03, 2.54mm_Pin_Headers:Interconnect_1x03, F.Cu at (115.6, 59.7)
- added J25: INTERCONNECT_1X03, 2.54mm_Pin_Headers:Interconnect_1x03, F.Cu at (115.6, 102.9)
- added J26: INTERCONNECT_1X03, 2.54mm_Pin_Headers:Interconnect_1x03, F.Cu at (115.6, 62.2)
- added J26: INTERCONNECT_1X03, 2.54mm_Pin_Headers:Interconnect_1x03, F.Cu at (115.6, 100.3)
- added J27: INTERCONNECT_1X03, 2.54mm_Pin_Headers:Interconnect_1x03, F.Cu at (115.6, 64.8)
- added J27: INTERCONNECT_1X03, 2.54mm_Pin_Headers:Interconnect_1x03, F.Cu at (115.6, 97.8)
- added J28: INTERCONNECT_1X03, 2.54mm_Pin_Headers:Interconnect_1x03, F.Cu at (115.6, 67.3)
- added J28: INTERCONNECT_1X03, 2.54mm_Pin_Headers:Interconnect_1x03, F.Cu at (115.6, 95.2)
- added J29: INTERCONNECT_1X03, 2.54mm_Pin_Headers:Interconnect_1x03, F.Cu at (115.6, 69.8)
- added J29: INTERCONNECT_1X03, 2.54mm_Pin_Headers:Interconnect_1x03, F.Cu at (115.6, 92.7)
- added J3: INTERCONNECT_1X03, 2.54mm_Pin_Headers:Interconnect_1x03, F.Cu at (123.2, 44.5)
- added J3: INTERCONNECT_1X03, 2.54mm_Pin_Headers:Interconnect_1x03, F.Cu at (123.2, 118.1)
- added J30: INTERCONNECT_1X03, 2.54mm_Pin_Headers:Interconnect_1x03, F.Cu at (115.6, 72.4)
- added J30: INTERCONNECT_1X03, 2.54mm_Pin_Headers:Interconnect_1x03, F.Cu at (115.6, 90.2)
- added J31: INTERCONNECT_1X03, 2.54mm_Pin_Headers:Interconnect_1x03, F.Cu at (115.6, 74.9)
- added J31: INTERCONNECT_1X03, 2.54mm_Pin_Headers:Interconnect_1x03, F.Cu at (115.6, 87.6)
- added J32: INTERCONNECT_1X03, 2.54mm_Pin_Headers:Interconnect_1x03, F.Cu at (115.6, 77.5)
- added J32: INTERCONNECT_1X03, 2.54mm_Pin_Headers:Interconnect_1x03, F.Cu at (115.6, 85.1)
- added J33: INTERCONNECT_1X03, 2.54mm_Pin_Headers:Interconnect_1x03, F.Cu at (102.9, 39.4)
- added J33: INTERCONNECT_1X03, 2.54mm_Pin_Headers:Interconnect_1x03, F.Cu at (102.9, 123.2)
- added J34: INTERCONNECT_1X03, 2.54mm_Pin_Headers:Interconnect_1x03, F.Cu at (102.9, 41.9)
- added J34: INTERCONNECT_1X03, 2.54mm_Pin_Headers:Interconnect_1x03, F.Cu at (102.9, 120.7)
- added J35: INTERCONNECT_1X03, 2.54mm_Pin_Headers:Interconnect_1x03, F.Cu at (102.9, 44.5)
- added J35: INTERCONNECT_1X03, 2.54mm_Pin_Headers:Interconnect_1x03, F.Cu at (102.9, 118.1)
- added J36: INTERCONNECT_1X03, 2.54mm_Pin_Headers:Interconnect_1x03, F.Cu at (102.9, 47.0)
- added J36: INTERCONNECT_1X03, 2.54mm_Pin_Headers:Interconnect_1x03, F.Cu at (102.9, 115.6)
- added J37: INTERCONNECT_1X03, 2.54mm_Pin_Headers:Interconnect_1x03, F.Cu at (102.9, 49.5)
- added J37: INTERCONNECT_1X03, 2.54mm_Pin_Headers:Interconnect_1x03, F.Cu at (102.9, 113.0)
- added J38: INTERCONNECT_1X03, 2.54mm_Pin_Headers:Interconnect_1x03, F.Cu at (102.9, 52.1)
- added J38: INTERCONNECT_1X03, 2.54mm_Pin_Headers:Interconnect_1x03, F.Cu at (102.9, 110.5)
- added J39: INTERCONNECT_1X03, 2.54mm_Pin_Headers:Interconnect_1x03, F.Cu at (102.9, 54.6)
- added J39: INTERCONNECT_1X03, 2.54mm_Pin_Headers:Interconnect_1x03, F.Cu at (102.9, 108.0)
- added J4: INTERCONNECT_1X03, 2.54mm_Pin_Headers:Interconnect_1x03, F.Cu at (123.2, 47.0)
- added J4: INTERCONNECT_1X03, 2.54mm_Pin_Headers:Interconnect_1x03, F.Cu at (123.2, 115.6)
- added J40: INTERCONNECT_1X03, 2.54mm_Pin_Headers:Interconnect_1x03, F.Cu at (102.9, 57.1)
- added J40: INTERCONNECT_1X03, 2.54mm_Pin_Headers:Interconnect_1x03, F.Cu at (102.9, 105.4)
- added J41: INTERCONNECT_1X03, 2.54mm_Pin_Headers:Interconnect_1x03, F.Cu at (102.9, 59.7)
- added J41: INTERCONNECT_1X03, 2.54mm_Pin_Headers:Interconnect_1x03, F.Cu at (102.9, 102.9)
- added J42: INTERCONNECT_1X03, 2.54mm_Pin_Headers:Interconnect_1x03, F.Cu at (102.9, 62.2)
- added J42: INTERCONNECT_1X03, 2.54mm_Pin_Headers:Interconnect_1x03, F.Cu at (102.9, 100.3)
- added J43: INTERCONNECT_1X03, 2.54mm_Pin_Headers:Interconnect_1x03, F.Cu at (102.9, 64.8)
- added J43: INTERCONNECT_1X03, 2.54mm_Pin_Headers:Interconnect_1x03, F.Cu at (102.9, 97.8)
- added J44: INTERCONNECT_1X03, 2.54mm_Pin_Headers:Interconnect_1x03, F.Cu at (102.9, 67.3)
- added J44: INTERCONNECT_1X03, 2.54mm_Pin_Headers:Interconnect_1x03, F.Cu at (102.9, 95.2)
- added J45: INTERCONNECT_1X03, 2.54mm_Pin_Headers:Interconnect_1x03, F.Cu at (102.9, 69.8)
- added J45: INTERCONNECT_1X03, 2.54mm_Pin_Headers:Interconnect_1x03, F.Cu at (102.9, 92.7)
- added J46: INTERCONNECT_1X03, 2.54mm_Pin_Headers:Interconnect_1x03, F.Cu at (102.9, 72.4)
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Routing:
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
